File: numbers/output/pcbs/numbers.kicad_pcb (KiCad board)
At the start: 2 copper layers, 120 x 98 mm, 55 parts

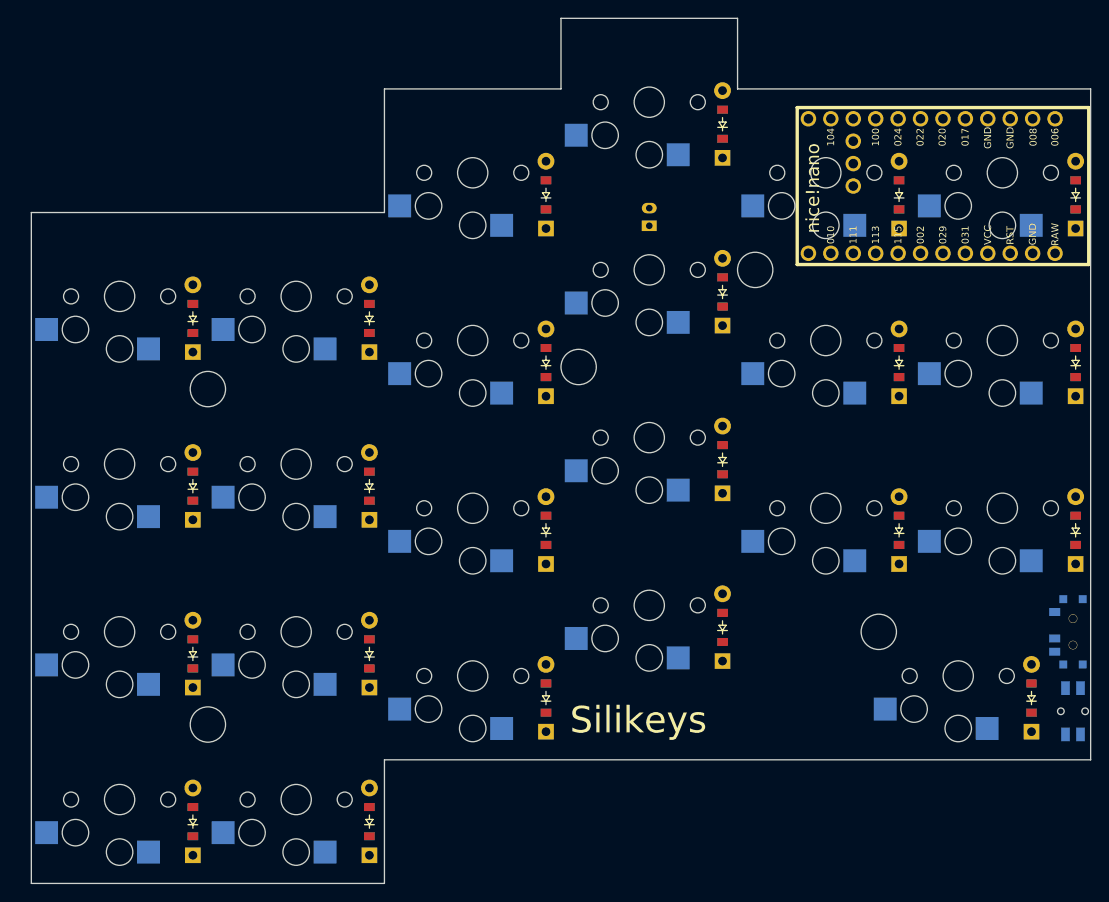
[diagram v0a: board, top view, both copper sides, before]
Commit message: added right, numbers, and altered left a little bit. I tweaked the location of the nice nano, all need to be retraced
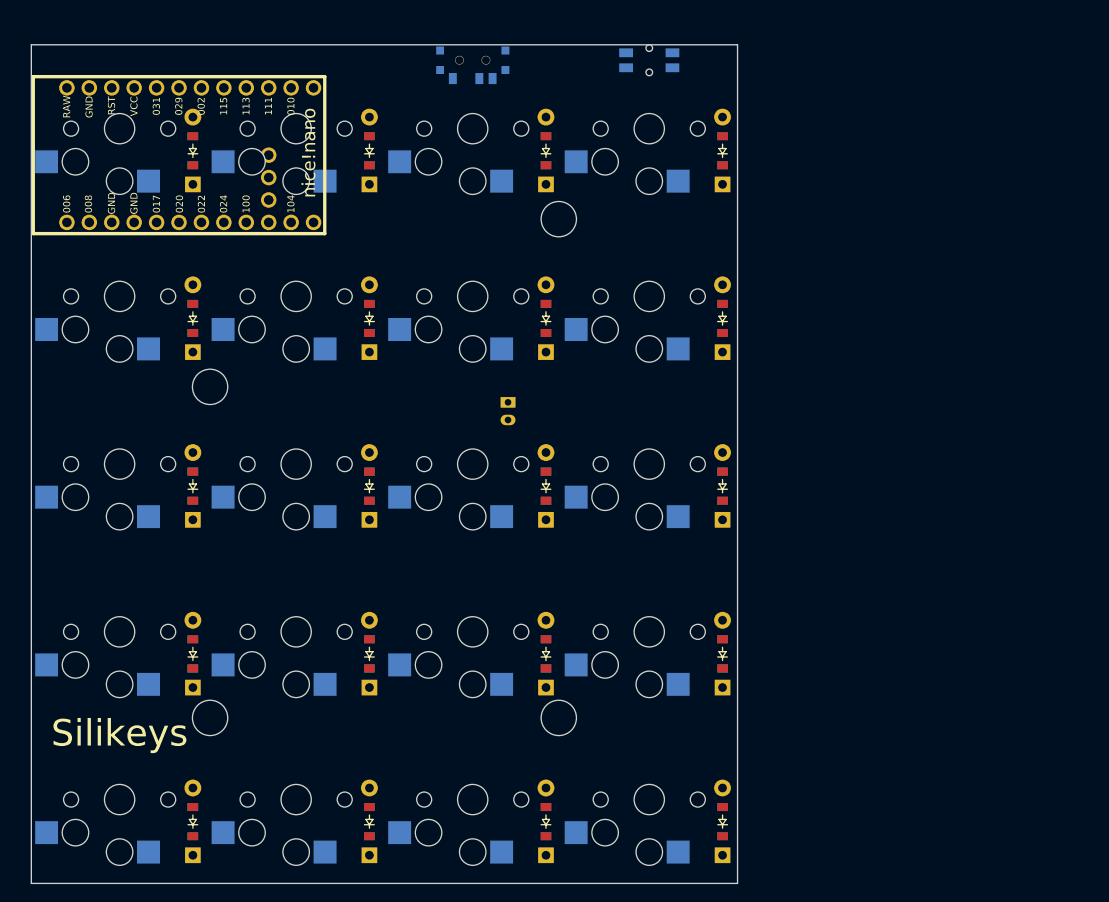
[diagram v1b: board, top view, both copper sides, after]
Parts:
- removed the ? at (110.0, 141.5)
- removed the ? at (110.0, 103.5)
- removed the ? at (152.0, 101.0)
- removed the ? at (186.0, 131.0)
- removed the ? at (172.0, 90.0)
- removed D21, D22, D23: , ComboDiode
- removed S21, S22, S23: , PG1350
- added ?: , HOLE_M2_TH, F.Cu at (110.2, 140.8)
- added ?: , HOLE_M2_TH, F.Cu at (110.2, 103.2)
- added ?: , HOLE_M2_TH, F.Cu at (149.8, 140.8)
- added ?: , HOLE_M2_TH, F.Cu at (149.8, 84.2)
- moved T1 93.9 mm to (140.0, 66.2), turned to 0 degrees
- moved B1 88.0 mm to (160.0, 66.2), turned to 0 degrees
- moved MCU1 84.1 mm to (108.0, 77.0), turned to 0 degrees
- moved D16 79.0 mm to (168.3, 152.5)
- moved S16 79.0 mm to (160.0, 150.0)
- moved D5 78.6 mm to (108.3, 76.5)
- moved S5 78.6 mm to (100.0, 74.0)
- moved D20 58.7 mm to (168.3, 76.5)
- moved S20 58.7 mm to (160.0, 74.0)
- moved D11 52.0 mm to (148.3, 152.5)
- moved D12 52.0 mm to (148.3, 133.5)
- moved S11 52.0 mm to (140.0, 150.0)
- moved S12 52.0 mm to (140.0, 131.0)
- moved D10 47.4 mm to (128.3, 76.5)
- moved D9 47.4 mm to (128.3, 95.5)
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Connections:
- net a_down renamed two_arrows
- net a_home renamed two_one
- net a_up renamed two_four
- net a_utility renamed first_numlock
- net d_down renamed three_seven
- net d_home renamed three_numlock
- net d_up renamed calc_arrows
- net d_utility renamed three_four
- net f_down renamed calc_one
- net f_home renamed calc_four
- net f_up renamed calc_seven
- net g_down renamed calc_numlock
- net s_down renamed two_numlock
- net s_home renamed three_arrows
- net s_up renamed three_one
- net s_utility renamed two_seven
- net shift_down renamed first_one
- net shift_home renamed first_four
- net shift_up renamed first_seven
- net shift_utility renamed first_arrows
- D10 pad 1: P002 -> P022
- D11 pad 1: P115 -> P029
- D12 pad 1: P113 -> P002
- D13 pad 1: P029 -> P115
- D14 pad 1: P002 -> P113
- D15 pad 1: P115 -> P022
- D16 pad 1: P113 -> P029
- D20 pad 1: P002 -> P022
- D5 pad 1: P029 -> P022
- D6 pad 1: P002 -> P029
- D7 pad 1: P115 -> P002
- D8 pad 1: P113 -> P115
- D9 pad 1: P029 -> P113
- S1 pad 1: P020 -> P017
- S10 pad 1: P024 -> P011
- S11 pad 1: P024 -> P100
- S12 pad 1: P024 -> P100
- S16 pad 1: P100 -> P024
- S17 pad 1: P011 -> P024
- S18 pad 1: P011 -> P024
- S19 pad 1: P011 -> P024
- S2 pad 1: P020 -> P017
- S20 pad 1: P017 -> P024
- S3 pad 1: P020 -> P017
- S4 pad 1: P020 -> P017
- S5 pad 1: P022 -> P017
- S6 pad 1: P022 -> P011
- S7 pad 1: P022 -> P011
- S8 pad 1: P022 -> P011
- S9 pad 1: P024 -> P011
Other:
- board size 120 x 98 mm -> 80 x 95 mm
